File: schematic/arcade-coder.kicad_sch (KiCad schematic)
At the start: 1 part, among them U1 ESP32-WROOM-32D

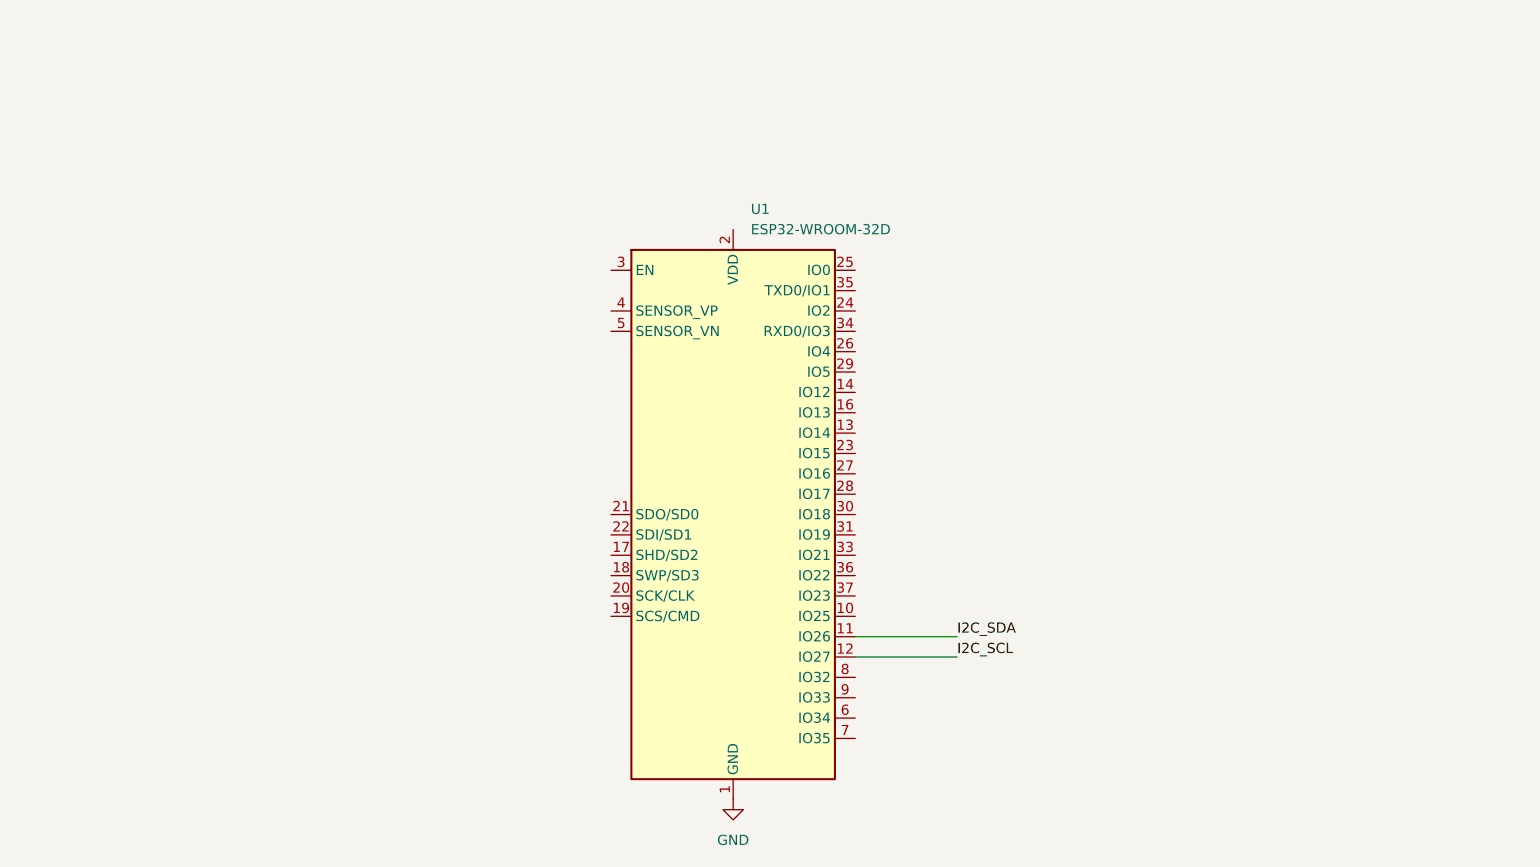
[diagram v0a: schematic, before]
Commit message: Added MCU page
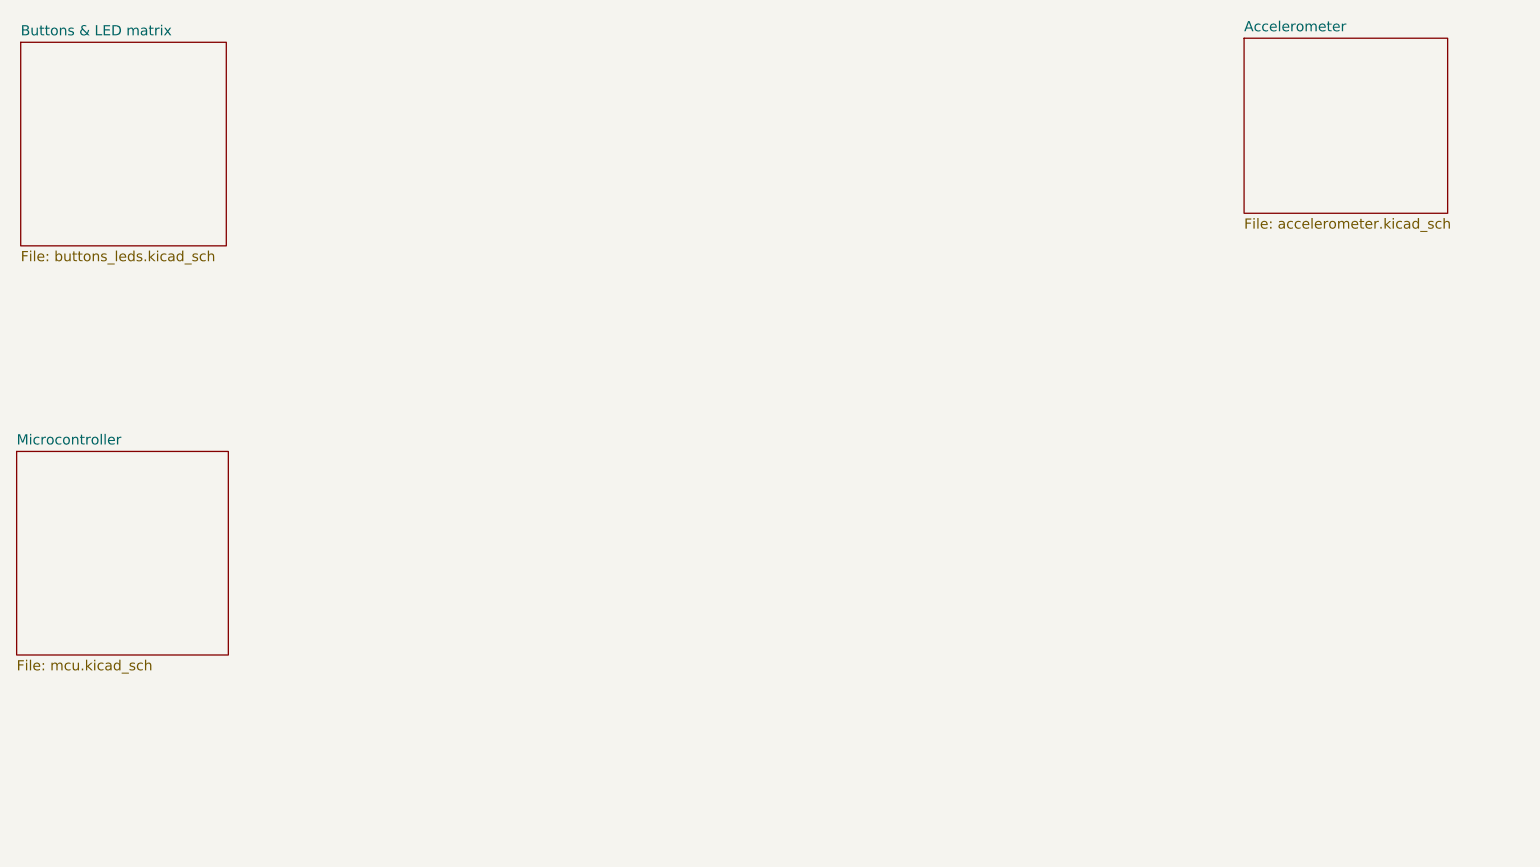
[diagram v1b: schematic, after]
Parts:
- removed U1: ESP32-WROOM-32D, RF_Module:ESP32-WROOM-32D, symbol RF_Module:ESP32-WROOM-32D
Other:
- added sheet Accelerometer (accelerometer.kicad_sch)
- added sheet Buttons & LED matrix (buttons_leds.kicad_sch)
- added sheet Microcontroller (mcu.kicad_sch)
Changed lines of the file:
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@@
 		(comment 1 "Reverse-engineered schematic")
 	)
-	(wire
-		(pts
-			(xy 154.94 127) (xy 167.64 127)
+	(sheet
+		(at 203.454 49.784)
+		(size 25.4 21.844)
+		(fields_autoplaced yes)
+		(stroke
+			(width 0.1524)
+			(type solid)
 		)
-		(stroke
-			(width 0)
-			(type default)
+		(fill
+			(color 0 0 0 0.0000)
 		)
-	)
-	(wire
-		(pts
-			(xy 154.94 124.46) (xy 167.64 124.46)
-		)
-		(stroke
-			(width 0)
-			(type default)
-		)
-	)
-	(label "I2C_SCL"
-		(at 167.64 127 0)
-		(fields_autoplaced yes)
-		(effects
-			(font
-				(size 1.27 1.27)
-			)
-			(justify left bottom)
-		)
-	)
-	(label "I2C_SDA"
-		(at 167.64 124.46 0)
-		(fields_autoplaced yes)
-		(effects
-			(font
-				(size 1.27 1.27)
-			)
-			(justify left bottom)
-		)
-	)
-	(symbol
-		(lib_id "RF_Module:ESP32-WROOM-32D")
-		(at 139.7 109.22 0)
-		(unit 1)
-		(exclude_from_sim no)
-		(in_bom yes)
-		(on_board yes)
-		(dnp no)
-		(fields_autoplaced yes)
-		(property "Reference" "U1"
-			(at 141.8941 71.12 0)
+		(property "Sheetname" "Accelerometer"
+			(at 203.454 49.0724 0)
 			(effects
 				(font
 					(size 1.27 1.27)
 				)
-				(justify left)
+				(justify left bottom)
 			)
 		)
-		(property "Value" "ESP32-WROOM-32D"
-			(at 141.8941 73.66 0)
+		(property "Sheetfile" "accelerometer.kicad_sch"
+			(at 203.454 72.2126 0)
 			(effects
 				(font
 					(size 1.27 1.27)
 				)
-				(justify left)
+				(justify left top)
 			)
 		)
-		(property "Footprint" "RF_Module:ESP32-WROOM-32D"
-			(at 156.21 143.51 0)
+		(instances
+			(project "arcade-coder"
+				(path "/38e9fd72-6eaf-40d3-a68c-7bd5bb0639e2"
+					(page "3")
+				)
+			)
+		)
+	)
+	(sheet
+		(at 50.292 101.346)
+		(size 26.416 25.4)
+		(fields_autoplaced yes)
+		(stroke
+			(width 0.1524)
+			(type solid)
+		)
+		(fill
+			(color 0 0 0 0.0000)
+		)
+		(property "Sheetname" "Microcontroller"
+			(at 50.292 100.6344 0)
 			(effects
 				(font
 					(size 1.27 1.27)
 				)
-				(hide yes)
+				(justify left bottom)
 			)
 		)
-		(property "Datasheet" "https://www.espressif.com/sites/default/files/documentation/esp32-wroom-32d_esp32-wroom-32u_datasheet_en.pdf"
-			(at 132.08 107.95 0)
+		(property "Sheetfile" "mcu.kicad_sch"
+			(at 50.292 127.3306 0)
 			(effects
 				(font
 					(size 1.27 1.27)
 				)
-				(hide yes)
+				(justify left top)
 			)
 		)
-		(property "Description" "RF Module, ESP32-D0WD SoC, Wi-Fi 802.11b/g/n, Bluetooth, BLE, 32-bit, 2.7-3.6V, onboard antenna, SMD"
-			(at 139.7 109.22 0)
+		(instances
+			(project "arcade-coder"
+				(path "/38e9fd72-6eaf-40d3-a68c-7bd5bb0639e2"
+					(page "4")
+				)
+			)
+		)
+	)
+	(sheet
+		(at 50.8 50.292)
+		(size 25.654 25.4)
+		(fields_autoplaced yes)
+		(stroke
+			(width 0.1524)
+			(type solid)
+		)
+		(fill
+			(color 0 0 0 0.0000)
+		)
+		(property "Sheetname" "Buttons & LED matrix"
+			(at 50.8 49.5804 0)
 			(effects
 				(font
 					(size 1.27 1.27)
 				)
-				(hide yes)
+				(justify left bottom)
 			)
 		)
-		(pin "8"
-		)
-		(pin "7"
-		)
-		(pin "9"
-		)
-		(pin "1"
-		)
-		(pin "16"
-		)
-		(pin "21"
-		)
-		(pin "20"
-		)
-		(pin "18"
-		)
-		(pin "2"
-		)
-		(pin "17"
-		)
-		(pin "35"
-		)
-		(pin "23"
-		)
-		(pin "33"
-		)
-		(pin "34"
-		)
-		(pin "22"
-		)
-		(pin "30"
-		)
-		(pin "25"
-		)
-		(pin "32"
-		)
-		(pin "6"
-		)
-		(pin "28"
-		)
-		(pin "37"
-		)
-		(pin "24"
-		)
-		(pin "27"
-		)
-		(pin "29"
-		)
-		(pin "31"
-		)
-		(pin "39"
-		)
-		(pin "38"
-		)
-		(pin "4"
-		)
-		(pin "5"
-		)
-		(pin "3"
-		)
-		(pin "11"
-		)
-		(pin "10"
-		)
-		(pin "13"
-		)
-		(pin "12"
-		)
-		(pin "26"
-		)
-		(pin "19"
-		)
-		(pin "14"
-		)
-		(pin "15"
-		)
-		(pin "36"
-		)
-		(instances
-			(project ""
-				(path "/38e9fd72-6eaf-40d3-a68c-7bd5bb0639e2"
-					(reference "U1")
-					(unit 1)
-				)
-			)
-		)
-	)
-	(symbol
-		(lib_id "power:GND")
-		(at 139.7 144.78 0)
-		(unit 1)
-		(exclude_from_sim no)
-		(in_bom yes)
-		(on_board yes)
-		(dnp no)
-		(fields_autoplaced yes)
-		(property "Reference" "#PWR01"
-			(at 139.7 151.13 0)
+		(property "Sheetfile" "buttons_leds.kicad_sch"
+			(at 50.8 76.2766 0)
 			(effects
 				(font
 					(size 1.27 1.27)
 				)
-				(hide yes)
+				(justify left top)
 			)
 		)
-		(property "Value" "GND"
-			(at 139.7 149.86 0)
-			(effects
-				(font
-					(size 1.27 1.27)
+		(instances
+			(project "arcade-coder"
+				(path "/38e9fd72-6eaf-40d3-a68c-7bd5bb0639e2"
+					(page "2")
 				)
 			)
-		)
-		(property "Footprint" ""
-			(at 139.7 144.78 0)
-			(effects
-				(font
-					(size 1.27 1.27)
-				)
-				(hide yes)
-			)
-		)
-		(property "Datasheet" ""
-			(at 139.7 144.78 0)
-			(effects
-				(font
-					(size 1.27 1.27)
-				)
-				(hide yes)
-			)
-		)
-		(property "Description" "Power symbol creates a global label with name \"GND\" , ground"
-			(at 139.7 144.78 0)
-			(effects
-				(font
-					(size 1.27 1.27)
-				)
-				(hide yes)
-			)
-		)
-		(pin "1"
-		)
-		(instances
-			(project ""
-				(path "/38e9fd72-6eaf-40d3-a68c-7bd5bb0639e2"
-					(reference "#PWR01")
-					(unit 1)
-				)
-			)
